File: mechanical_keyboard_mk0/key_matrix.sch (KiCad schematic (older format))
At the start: 8 parts, among them SW1 SW_SPST, SW2 SW_SPST, SW3 SW_SPST, SW4 SW_SPST

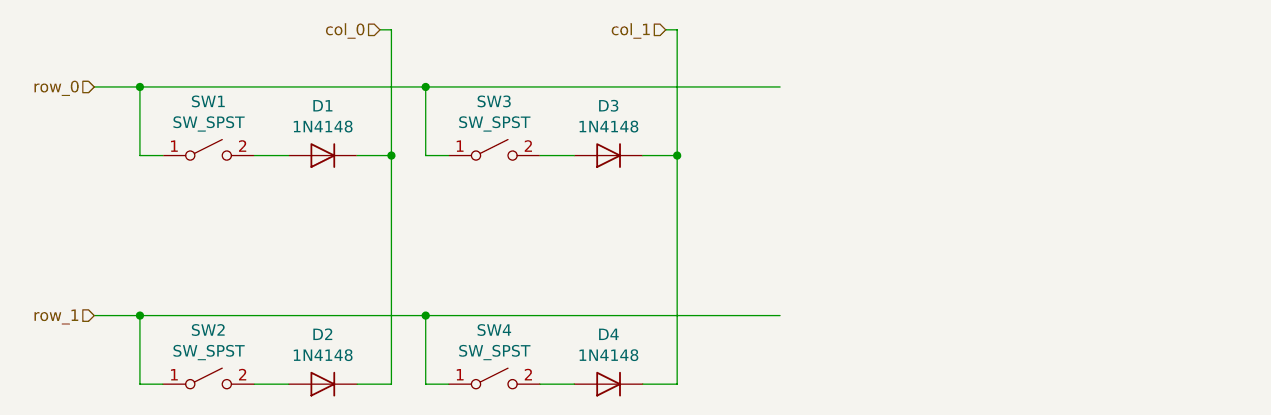
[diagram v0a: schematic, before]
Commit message: Updated to 2 rows.
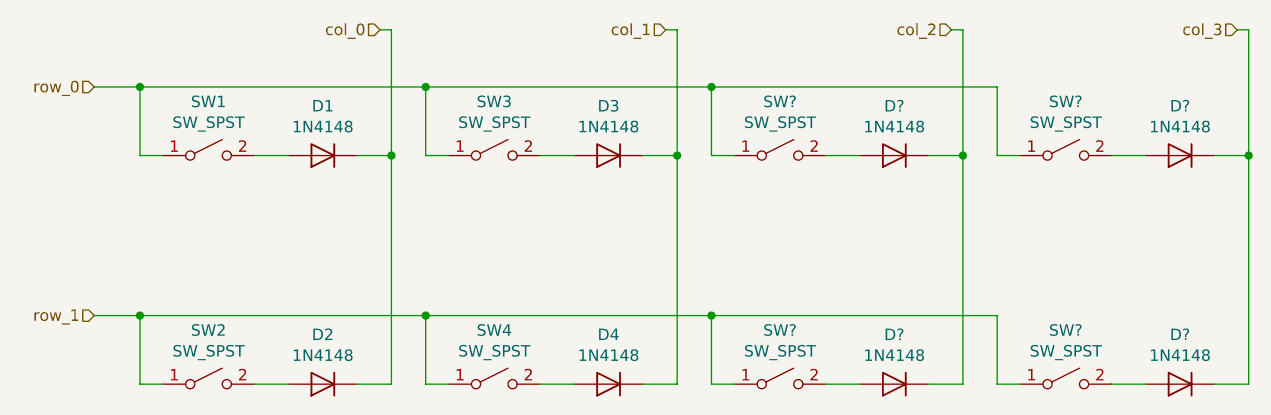
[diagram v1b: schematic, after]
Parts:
- added D? (x4): 1N4148, Diode_THT:D_DO-35_SOD27_P7.62mm_Horizontal, symbol Diode:1N4148
- added SW? (x4): SW_SPST, Button_Switch_Keyboard:SW_Cherry_MX_1.00u_PCB, symbol Switch:SW_SPST
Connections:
- net labels added: col_2, col_3
- wire segments 28 -> 52
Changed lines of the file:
@@
 	5550 1750 5500 1750
 Wire Wire Line
-	4450 2000 6000 2000
+	4450 2000 5700 2000
 Connection ~ 4450 2000
 Wire Wire Line
-	4450 3000 6000 3000
+	4450 3000 5700 3000
 Connection ~ 4450 3000
 Wire Wire Line
@@
 Wire Wire Line
 	5550 2300 5550 3300
+Text HLabel 6750 1750 0    50   Input ~ 0
+col_2
+$Comp
+L Switch:SW_SPST SW?
+U 1 1 5CEFAEF4
+P 6000 2300
+F 0 "SW?" H 6000 2535 50  0000 C CNN
+F 1 "SW_SPST" H 6000 2444 50  0000 C CNN
+F 2 "Button_Switch_Keyboard:SW_Cherry_MX_1.00u_PCB" H 6000 2300 50  0001 C CNN
+F 3 "~" H 6000 2300 50  0001 C CNN
+	1    6000 2300
+	1    0    0    -1
+$EndComp
+$Comp
+L Diode:1N4148 D?
+U 1 1 5CEFAEFA
+P 6500 2300
+F 0 "D?" H 6500 2084 50  0000 C CNN
+F 1 "1N4148" H 6500 2175 50  0000 C CNN
+F 2 "Diode_THT:D_DO-35_SOD27_P7.62mm_Horizontal" H 6500 2125 50  0001 C CNN
+F 3 "https://assets.nexperia.com/documents/data-sheet/1N4148_1N4448.pdf" H 6500 2300 50  0001 C CNN
+	1    6500 2300
+	-1   0    0    1
+$EndComp
+Wire Wire Line
+	5700 2000 5700 2300
+Wire Wire Line
+	5700 2300 5800 2300
+Wire Wire Line
+	6200 2300 6350 2300
+$Comp
+L Switch:SW_SPST SW?
+U 1 1 5CEFAF04
+P 6000 3300
+F 0 "SW?" H 6000 3535 50  0000 C CNN
+F 1 "SW_SPST" H 6000 3444 50  0000 C CNN
+F 2 "Button_Switch_Keyboard:SW_Cherry_MX_1.00u_PCB" H 6000 3300 50  0001 C CNN
+F 3 "~" H 6000 3300 50  0001 C CNN
+	1    6000 3300
+	1    0    0    -1
+$EndComp
+$Comp
+L Diode:1N4148 D?
+U 1 1 5CEFAF0A
+P 6500 3300
+F 0 "D?" H 6500 3084 50  0000 C CNN
+F 1 "1N4148" H 6500 3175 50  0000 C CNN
+F 2 "Diode_THT:D_DO-35_SOD27_P7.62mm_Horizontal" H 6500 3125 50  0001 C CNN
+F 3 "https://assets.nexperia.com/documents/data-sheet/1N4148_1N4448.pdf" H 6500 3300 50  0001 C CNN
+	1    6500 3300
+	-1   0    0    1
+$EndComp
+Wire Wire Line
+	5700 3000 5700 3300
+Wire Wire Line
+	5700 3300 5800 3300
+Wire Wire Line
+	6200 3300 6350 3300
+Wire Wire Line
+	6800 1750 6750 1750
+Wire Wire Line
+	6800 3300 6650 3300
+Wire Wire Line
+	6800 1750 6800 2300
+Wire Wire Line
+	6650 2300 6800 2300
+Connection ~ 6800 2300
+Wire Wire Line
+	6800 2300 6800 3300
+Connection ~ 5700 2000
+Connection ~ 5700 3000
+Text HLabel 8000 1750 0    50   Input ~ 0
+col_3
+$Comp
+L Switch:SW_SPST SW?
+U 1 1 5CF0C20A
+P 7250 2300
+F 0 "SW?" H 7250 2535 50  0000 C CNN
+F 1 "SW_SPST" H 7250 2444 50  0000 C CNN
+F 2 "Button_Switch_Keyboard:SW_Cherry_MX_1.00u_PCB" H 7250 2300 50  0001 C CNN
+F 3 "~" H 7250 2300 50  0001 C CNN
+	1    7250 2300
+	1    0    0    -1
+$EndComp
+$Comp
+L Diode:1N4148 D?
+U 1 1 5CF0C210
+P 7750 2300
+F 0 "D?" H 7750 2084 50  0000 C CNN
+F 1 "1N4148" H 7750 2175 50  0000 C CNN
+F 2 "Diode_THT:D_DO-35_SOD27_P7.62mm_Horizontal" H 7750 2125 50  0001 C CNN
+F 3 "https://assets.nexperia.com/documents/data-sheet/1N4148_1N4448.pdf" H 7750 2300 50  0001 C CNN
+	1    7750 2300
+	-1   0    0    1
+$EndComp
+Wire Wire Line
+	6950 2000 6950 2300
+Wire Wire Line
+	6950 2300 7050 2300
+Wire Wire Line
+	7450 2300 7600 2300
+$Comp
+L Switch:SW_SPST SW?
+U 1 1 5CF0C219
+P 7250 3300
+F 0 "SW?" H 7250 3535 50  0000 C CNN
+F 1 "SW_SPST" H 7250 3444 50  0000 C CNN
+F 2 "Button_Switch_Keyboard:SW_Cherry_MX_1.00u_PCB" H 7250 3300 50  0001 C CNN
+F 3 "~" H 7250 3300 50  0001 C CNN
+	1    7250 3300
+	1    0    0    -1
+$EndComp
+$Comp
+L Diode:1N4148 D?
+U 1 1 5CF0C21F
+P 7750 3300
+F 0 "D?" H 7750 3084 50  0000 C CNN
+F 1 "1N4148" H 7750 3175 50  0000 C CNN
+F 2 "Diode_THT:D_DO-35_SOD27_P7.62mm_Horizontal" H 7750 3125 50  0001 C CNN
+F 3 "https://assets.nexperia.com/documents/data-sheet/1N4148_1N4448.pdf" H 7750 3300 50  0001 C CNN
+	1    7750 3300
+	-1   0    0    1
+$EndComp
+Wire Wire Line
+	6950 3000 6950 3300
+Wire Wire Line
+	6950 3300 7050 3300
+Wire Wire Line
+	7450 3300 7600 3300
+Wire Wire Line
+	8050 1750 8000 1750
+Wire Wire Line
+	8050 3300 7900 3300
+Wire Wire Line
+	8050 1750 8050 2300
+Wire Wire Line
+	7900 2300 8050 2300
+Connection ~ 8050 2300
+Wire Wire Line
+	8050 2300 8050 3300
+Wire Wire Line
+	5700 3000 6950 3000
+Wire Wire Line
+	5700 2000 6950 2000
 $EndSCHEMATC

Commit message: Updated layout, created first output job.
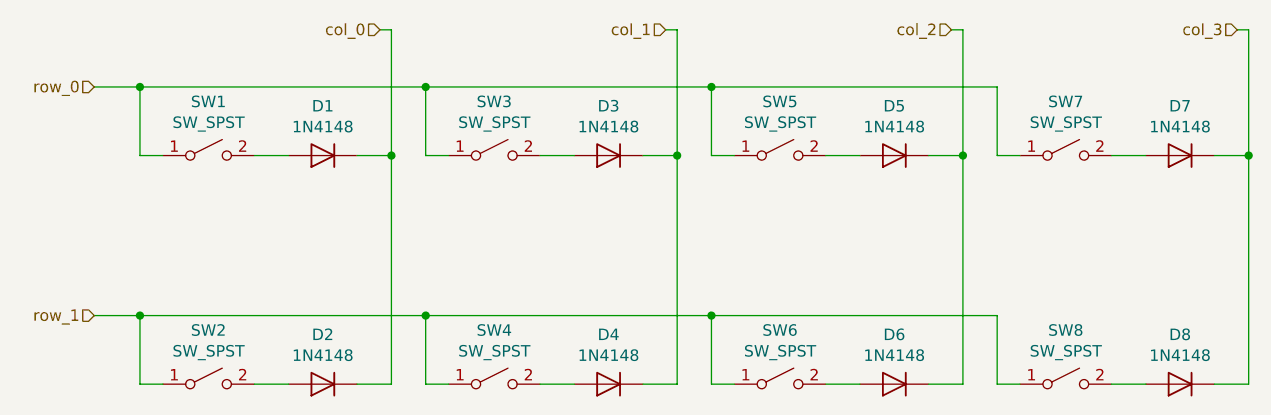
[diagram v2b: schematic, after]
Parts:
- gave numbers to parts that had none: 8
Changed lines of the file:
@@
 col_2
 $Comp
-L Switch:SW_SPST SW?
+L Switch:SW_SPST SW5
 U 1 1 5CEFAEF4
 P 6000 2300
-F 0 "SW?" H 6000 2535 50  0000 C CNN
+F 0 "SW5" H 6000 2535 50  0000 C CNN
 F 1 "SW_SPST" H 6000 2444 50  0000 C CNN
 F 2 "Button_Switch_Keyboard:SW_Cherry_MX_1.00u_PCB" H 6000 2300 50  0001 C CNN
@@
 $EndComp
 $Comp
-L Diode:1N4148 D?
+L Diode:1N4148 D5
 U 1 1 5CEFAEFA
 P 6500 2300
-F 0 "D?" H 6500 2084 50  0000 C CNN
+F 0 "D5" H 6500 2084 50  0000 C CNN
 F 1 "1N4148" H 6500 2175 50  0000 C CNN
 F 2 "Diode_THT:D_DO-35_SOD27_P7.62mm_Horizontal" H 6500 2125 50  0001 C CNN
@@
 	6200 2300 6350 2300
 $Comp
-L Switch:SW_SPST SW?
+L Switch:SW_SPST SW6
 U 1 1 5CEFAF04
 P 6000 3300
-F 0 "SW?" H 6000 3535 50  0000 C CNN
+F 0 "SW6" H 6000 3535 50  0000 C CNN
 F 1 "SW_SPST" H 6000 3444 50  0000 C CNN
 F 2 "Button_Switch_Keyboard:SW_Cherry_MX_1.00u_PCB" H 6000 3300 50  0001 C CNN
@@
 $EndComp
 $Comp
-L Diode:1N4148 D?
+L Diode:1N4148 D6
 U 1 1 5CEFAF0A
 P 6500 3300
-F 0 "D?" H 6500 3084 50  0000 C CNN
+F 0 "D6" H 6500 3084 50  0000 C CNN
 F 1 "1N4148" H 6500 3175 50  0000 C CNN
 F 2 "Diode_THT:D_DO-35_SOD27_P7.62mm_Horizontal" H 6500 3125 50  0001 C CNN
@@
 col_3
 $Comp
-L Switch:SW_SPST SW?
+L Switch:SW_SPST SW7
 U 1 1 5CF0C20A
 P 7250 2300
-F 0 "SW?" H 7250 2535 50  0000 C CNN
+F 0 "SW7" H 7250 2535 50  0000 C CNN
 F 1 "SW_SPST" H 7250 2444 50  0000 C CNN
 F 2 "Button_Switch_Keyboard:SW_Cherry_MX_1.00u_PCB" H 7250 2300 50  0001 C CNN
@@
 $EndComp
 $Comp
-L Diode:1N4148 D?
+L Diode:1N4148 D7
 U 1 1 5CF0C210
 P 7750 2300
-F 0 "D?" H 7750 2084 50  0000 C CNN
+F 0 "D7" H 7750 2084 50  0000 C CNN
 F 1 "1N4148" H 7750 2175 50  0000 C CNN
 F 2 "Diode_THT:D_DO-35_SOD27_P7.62mm_Horizontal" H 7750 2125 50  0001 C CNN
@@
 	7450 2300 7600 2300
 $Comp
-L Switch:SW_SPST SW?
+L Switch:SW_SPST SW8
 U 1 1 5CF0C219
 P 7250 3300
-F 0 "SW?" H 7250 3535 50  0000 C CNN
+F 0 "SW8" H 7250 3535 50  0000 C CNN
 F 1 "SW_SPST" H 7250 3444 50  0000 C CNN
 F 2 "Button_Switch_Keyboard:SW_Cherry_MX_1.00u_PCB" H 7250 3300 50  0001 C CNN
@@
 $EndComp
 $Comp
-L Diode:1N4148 D?
+L Diode:1N4148 D8
 U 1 1 5CF0C21F
 P 7750 3300
-F 0 "D?" H 7750 3084 50  0000 C CNN
+F 0 "D8" H 7750 3084 50  0000 C CNN
 F 1 "1N4148" H 7750 3175 50  0000 C CNN
 F 2 "Diode_THT:D_DO-35_SOD27_P7.62mm_Horizontal" H 7750 3125 50  0001 C CNN
